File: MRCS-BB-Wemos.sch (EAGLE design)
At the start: 4 parts

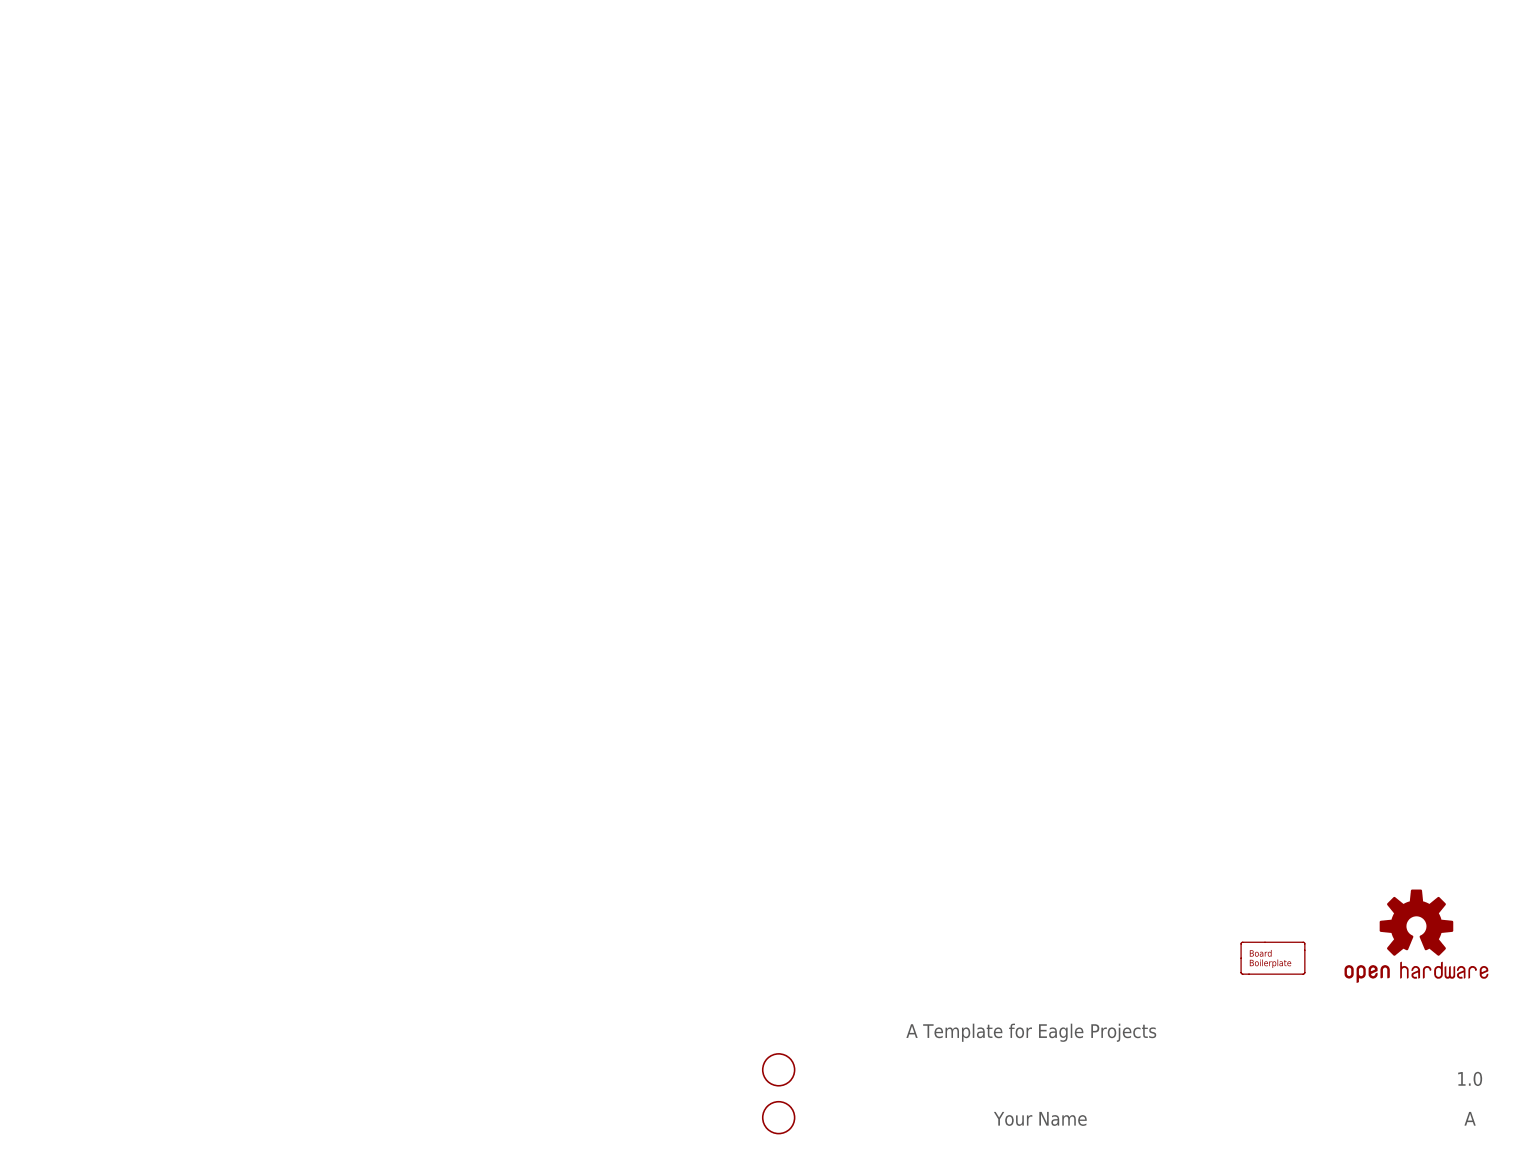
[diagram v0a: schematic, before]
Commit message: moved BB-Wemos from EAGLE directory
we made a short run of these, which Dennis Drumheller bought.
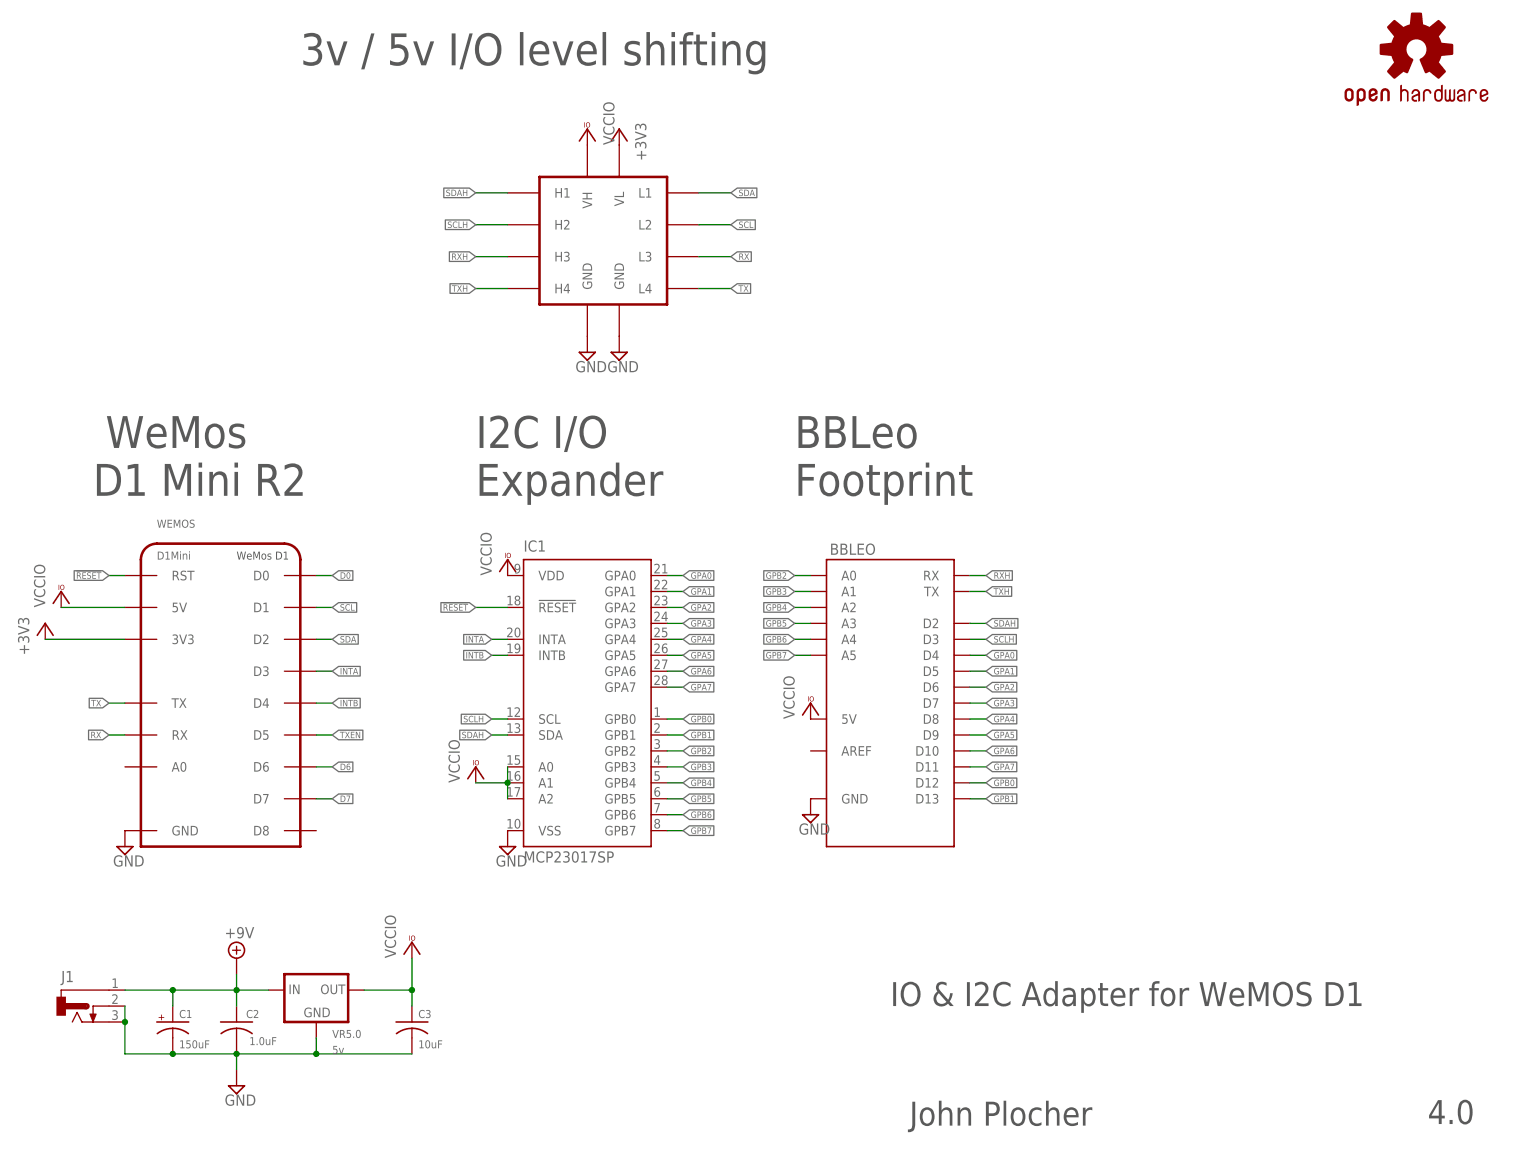
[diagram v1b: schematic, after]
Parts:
- removed BOARD1: BOARD80X100, SPCoast:BOARD80X100
- removed FID1, FID2: FIDUCIAL, SPCoast:FIDUCIAL
- added BBLEO: (no value), SPCoast:ARDUINO-BBLEO
- added C1: 150uF, SPCoast:CAP-POLPTH-5MM
- added C2: 1.0uF, SPCoast:CAPPTH1
- added C3: 10uF, SPCoast:CAPPTH1
- added IC1: MCP23017SP, microchip:MCP23017SP
- added J1: (no value), SPCoast:CONNECTOR-DC-POWER-RA
- added LABEL1: 7-12vDC, SPCoast-minimal:POWER_LABEL
- added LS2: (no value), SPCoast:I2C-LEVELSHIFTER
- added VR5.0: 5v, SPCoast:VREG-PTH-FLAT-5
- added WEMOS: D1Mini, SPCoast:WEMOS-D1V1
- OSHW1: value DOC-OSHW-LOGO-M -> OSHW-LOGOL; device SPCoast:DOC-OSHW-LOGO-M -> SparkFun:OSHW-LOGOL
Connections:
- new net !RESET: IC1.!RESET, WEMOS.RST
- new net +3V3: LS2.VL, WEMOS.3V3
- new net +9V: C1.+, C2.1, J1.1, VR5.0.IN
- new net D0: WEMOS.D0
- new net D6: WEMOS.D6
- new net D7: WEMOS.D7
- new net GND: BBLEO.GND, C1.-, C2.2, C3.2, IC1.VSS, J1.2, J1.3, LS2.GND@0, LS2.GND@1, VR5.0.GND, WEMOS.GND
- new net GPA0: BBLEO.D4, IC1.GPA0
- new net GPA1: BBLEO.D5, IC1.GPA1
- new net GPA2: BBLEO.D6, IC1.GPA2
- new net GPA3: BBLEO.D7, IC1.GPA3
- new net GPA4: BBLEO.D8, IC1.GPA4
- new net GPA5: BBLEO.D9, IC1.GPA5
- new net GPA6: BBLEO.D10, IC1.GPA6
- new net GPA7: BBLEO.D11, IC1.GPA7
- new net GPB0: BBLEO.D12, IC1.GPB0
- new net GPB1: BBLEO.D13, IC1.GPB1
- new net GPB2: BBLEO.A0, IC1.GPB2
- new net GPB3: BBLEO.A1, IC1.GPB3
- new net GPB4: BBLEO.A2, IC1.GPB4
- new net GPB5: BBLEO.A3, IC1.GPB5
- new net GPB6: BBLEO.A4, IC1.GPB6
- new net GPB7: BBLEO.A5, IC1.GPB7
- new net INTA: IC1.INTA, WEMOS.D3
- new net INTB: IC1.INTB, WEMOS.D4
- new net RX: LS2.L3, WEMOS.RX
- new net RXH: BBLEO.RX, LS2.H3
- new net SCL: LS2.L2, WEMOS.D1
- new net SCLH: BBLEO.D3, IC1.SCL, LS2.H2
- new net SDA: LS2.L1, WEMOS.D2
- new net SDAH: BBLEO.D2, IC1.SDA, LS2.H1
- new net TX: LS2.L4, WEMOS.TX
- new net TXEN: WEMOS.D5
- new net TXH: BBLEO.TX, LS2.H4
- new net VCCIO: BBLEO.5V, C3.1, IC1.A0, IC1.A1, IC1.A2, IC1.VDD, LS2.VH, VR5.0.OUT, WEMOS.5V
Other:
- note added: "3v / 5v I/O level shifting"
- note added: "4.0"
- note added: "BBLeo Footprint"
- note added: "I2C I/O Expander"
- note added: "IO & I2C Adapter for WeMOS D1"
- note added: "John Plocher"
- note added: "Processor carrier board for WeMOS D1 Breaks out 5v I2C, IO4 style header for access to Serial & I2C"
- note added: "WeMos D1 Mini R2"
- note removed: "1.0"
- note removed: "A"
- note removed: "A Template for Eagle Projects"
- note removed: "Your Name"
